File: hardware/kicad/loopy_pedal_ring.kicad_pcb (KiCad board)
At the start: 2 copper layers, 68 x 68 mm, 25 parts, among them J1 Conn_01x08

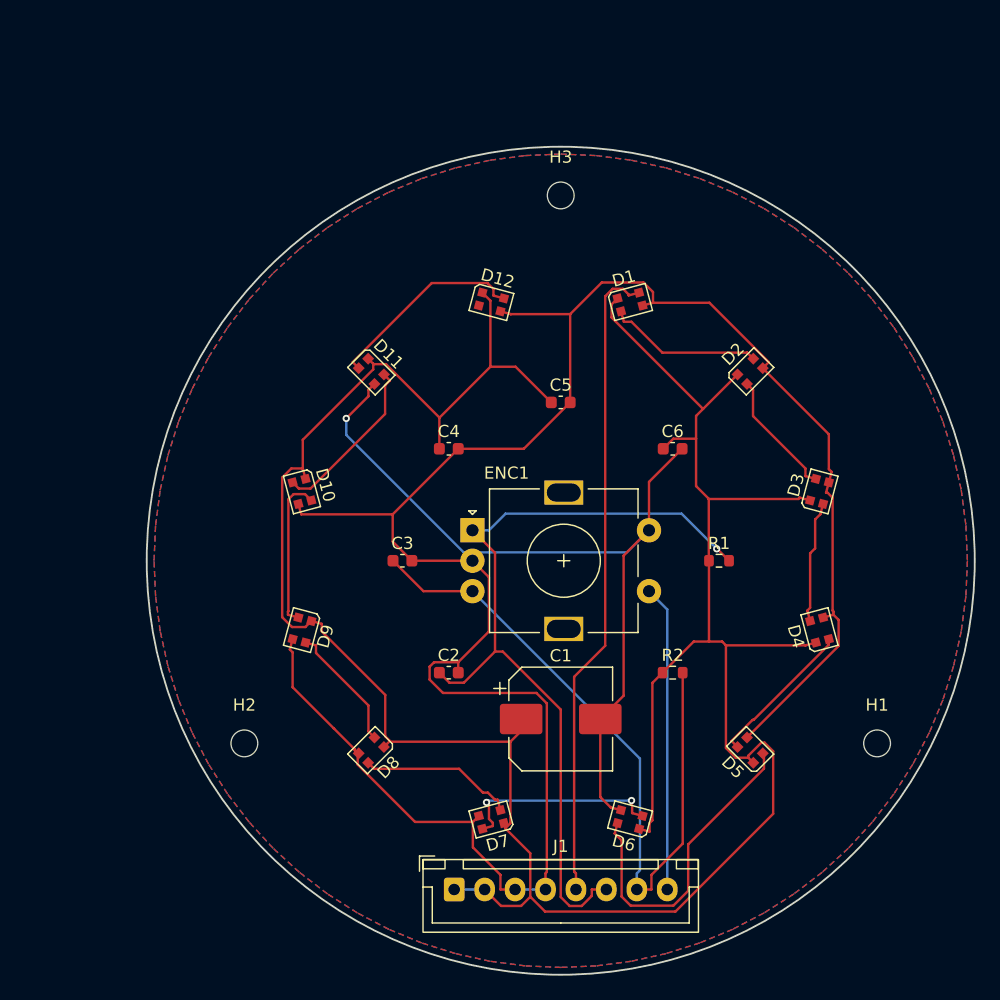
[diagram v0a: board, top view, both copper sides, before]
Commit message: feat(hardware): THT Loopy pedal main + ring boards, fab-ready
Through-hole MIDI looper foot-pedal: two KiCad 10 boards generated from
SKiDL + a scripted place/route pipeline, ready for JLCPCB bare-board fab.

Main board (94x96mm):
- Arduino Pro Micro (ATmega32U4) native USB-MIDI, buffered DIN MIDI OUT
  (74AHCT125), opto-isolated DIN MIDI IN (H11L1)
- 9V centre-negative barrel -> reverse-protection Schottky + TVS -> buck
  (+5V_LED for the LED ring); Pro Micro powered via RAW (onboard reg -> VCC)
- 10 footswitch headers, faceplate RESET (J20) + 6-pin ICSP (J21) recovery
- Fully silk-labelled (functions + component values), 4x M3 GND-bonded holes

Ring board (60mm round):
- Hosts an off-the-shelf 16-LED WS2812 NeoPixel module + EC11 encoder,
  8-pin link to the main board; 4-pad module mount (DIN/+5V/GND + DOUT post)

Both boards DRC-clean; gerbers + BOM/CPL in fab/. Vendored footprints and
3D models in loopy.pretty/. Plan-of-record in loopy_pedal_pcb_tht_plan.md.
Firmware skeleton (USB-MIDI + Serial1 DIN + footswitch debounce) in firmware/.
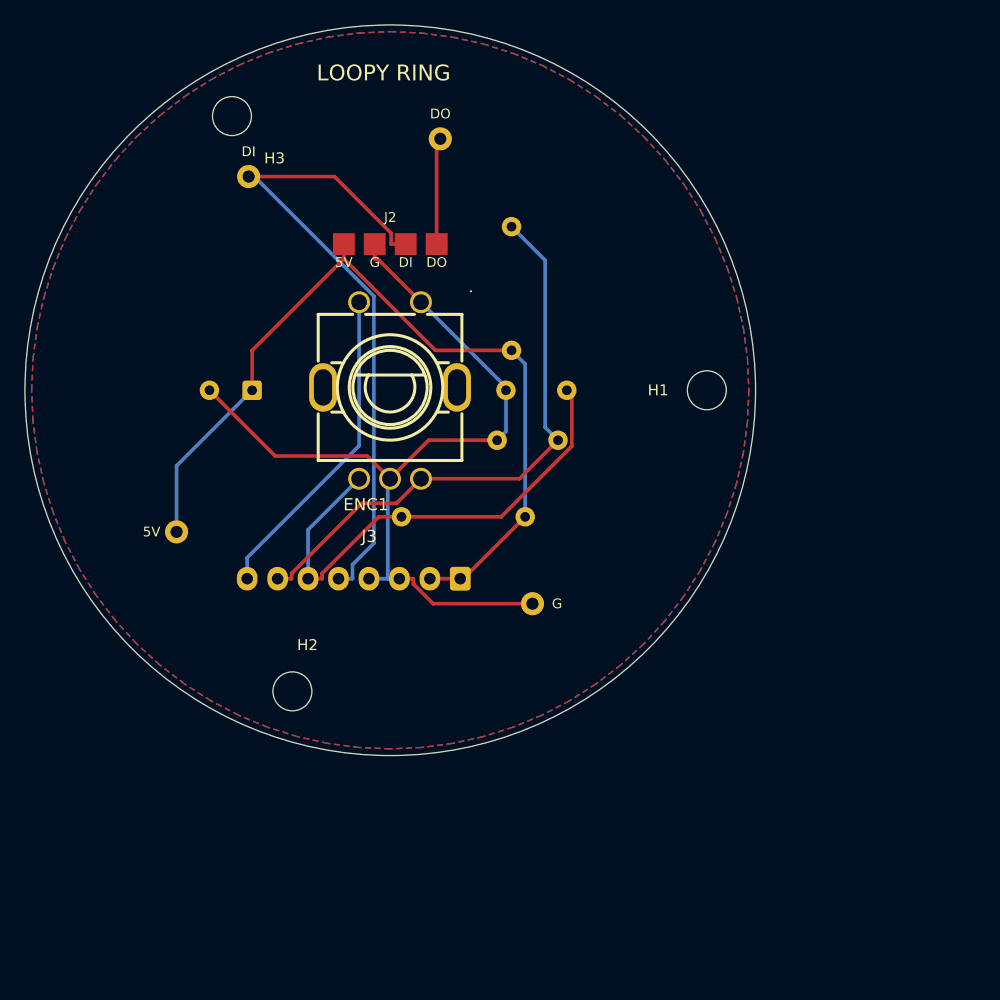
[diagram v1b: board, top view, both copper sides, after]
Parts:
- removed C4, C5, C6: 100nF, C_0603_1608Metric
- removed D1, D10, D11, D12, D2, D3, D4, D5, D6, D7, D8, D9: WS2812B, LED_WS2812B-2020_PLCC4_2.0x2.0mm
- added J2: NEOPIXEL, WirePads_1x04, F.Cu at (36.0, 24.0)
- added J3: RINGPINS, ModuleMountPads_4, F.Cu at (36.0, 36.0)
- added RING1: NeoPixel16, NeoPixel_Ring16, F.Cu at (36.0, 36.0)
- C1: value 1000uF -> 470uF; footprint CP_Elec_8x10 -> CP_Radial_D8.0mm_P3.50mm; moved to B.Cu
- C2, C3: footprint C_0603_1608Metric -> C_Disc_D5.0mm_W2.5mm_P5.00mm; moved to B.Cu
- ENC1: footprint RotaryEncoder_Alps_EC11E-Switch_Vertical_H20mm -> RotaryEncoder_EC11
- H1, H2, H3: value MountingHole_2.2mm_M2 -> MountingHole_3.2mm_M3; footprint MountingHole_2.2mm_M2 -> MountingHole_3.2mm_M3
- J1: moved to B.Cu
- R1, R2: footprint R_0603_1608Metric -> R_Axial_DIN0207_L6.3mm_D2.5mm_P10.16mm_Horizontal; moved to B.Cu
- moved C1 37.0 mm to (24.7, 36.0), turned to 180 degrees
- moved H1 32.2 mm to (62.0, 36.0)
- moved R2 29.6 mm to (46.0, 32.7), turned to 90 degrees
- moved H3 27.8 mm to (23.0, 13.5)
- moved J1 25.5 mm to (41.8, 51.5), turned to 180 degrees
- moved C2 25.1 mm to (50.5, 36.0), turned to 180 degrees
- moved R1 16.3 mm to (47.1, 46.4), turned to 180 degrees
- moved C3 16.2 mm to (49.8, 40.1), turned to 180 degrees
- moved ENC1 13.3 mm to (36.0, 36.0)
- moved H2 5.82 mm to (28.0, 60.7)
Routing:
- net GND: track 252.7 -> 71.8 mm, vias 1 -> 0
- net +5V_LED: track 223.1 -> 70.3 mm
- net ENC_A: track 67.6 -> 41.1 mm, vias 1 -> 0
- net RING_D5: track 26.5 -> 0.00 mm
- net RING_D6: track 17.0 -> 0.00 mm, vias 2 -> 0
- net RING_D11: track 16.6 -> 0.00 mm
- net RING_D10: track 14.0 -> 0.00 mm
- net RING_D1: track 12.8 -> 0.00 mm
- net RING_D7: track 12.8 -> 0.00 mm
- net RING_D9: track 12.7 -> 0.00 mm
- net RING_D4: track 12.4 -> 0.00 mm
- net ENC_B: track 57.9 -> 47.1 mm
- net RING_D2: track 10.4 -> 0.00 mm
- net RING_D8: track 10.4 -> 0.00 mm
- net RING_D3: track 10.1 -> 0.00 mm
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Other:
- board size 68 x 68 mm -> 60 x 60 mm
- board text added: "LOOPY RING"

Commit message: feat(hardware): main-board respin — on-board buck, floorplan, wide rails + ground planes
Reworked the loopy_pedal main board:
- MP1584 buck mounts flat on its own footprint (loopy:BuckModule_MP1584 + STEP),
  no longer a 1x4 header; fixed the SW_TRACK4<->R7/R8 short by relocating the
  A3-sense divider; added local decoupling C11/C16 for U1/U2.
- Floorplan: power grouped in the bottom band, MIDI on the right, Pro Micro on
  the left (USB accessible); force-directed placement + Freerouting.
- Power nets 0.8mm / +5V 0.5mm net classes, dual F.Cu+B.Cu ground planes.
- Ring board: component values onto the silkscreen.
DRC: main + ring both 0 violations, 0 unconnected.
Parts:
- ENC1: value RotaryEncoder_Switch -> EC11
- J1: value Conn_01x08 -> JST-XH 8P
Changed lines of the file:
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@@
 			)
 		)
-		(property "Value" "RotaryEncoder_Switch"
-			(at 0 11.25 0)
-			(layer "F.Fab")
-			(effects
-				(font
-					(size 1 1)
+		(property "Value" "EC11"
+			(at -11.9825 -5.0175 0)
+			(layer "F.SilkS")
+			(effects
+				(font
+					(size 0.8 0.8)
 					(thickness 0.15)
 				)
@@
 		(property "Value" "NEOPIXEL"
 			(at 0 2.6 0)
-			(layer "F.Fab")
-			(hide yes)
+			(layer "F.SilkS")
 			(effects
 				(font
@@
 		)
 		(property "Value" "RINGPINS"
-			(at 0 15 0)
-			(layer "F.Fab")
-			(hide yes)
-			(effects
-				(font
-					(size 1 1)
+			(at 12 -5 0)
+			(layer "F.SilkS")
+			(effects
+				(font
+					(size 0.8 0.8)
 					(thickness 0.15)
 				)
@@
 		(property "Value" "NeoPixel16"
 			(at 0 25 0)
-			(layer "F.Fab")
-			(hide yes)
+			(layer "F.SilkS")
 			(effects
 				(font
@@
 		)
 		(property "Value" "100nF"
-			(at 2.5 -2.5 0)
-			(layer "B.Fab")
-			(effects
-				(font
-					(size 1 1)
+			(at 0 6 0)
+			(layer "B.SilkS")
+			(effects
+				(font
+					(size 0.8 0.8)
 					(thickness 0.15)
 				)
@@
 		)
 		(property "Value" "10k"
-			(at 5.08 -2.37 0)
-			(layer "B.Fab")
-			(effects
-				(font
-					(size 1 1)
+			(at -5.92 4.3923 0)
+			(layer "B.SilkS")
+			(effects
+				(font
+					(size 0.8 0.8)
 					(thickness 0.15)
 				)
@@
 			)
 		)
-		(property "Value" "Conn_01x08"
+		(property "Value" "JST-XH 8P"
 			(at 8.75 -4.6 0)
-			(layer "B.Fab")
+			(layer "B.SilkS")
 			(effects
 				(font
@@
 		(property "Value" "10k"
 			(at 5.08 -2.37 90)
-			(layer "B.Fab")
+			(layer "B.SilkS")
 			(effects
 				(font
@@
 		(property "Value" "100nF"
 			(at 2.5 -2.5 0)
-			(layer "B.Fab")
+			(layer "B.SilkS")
 			(effects
 				(font
@@
 		(property "Value" "470uF"
 			(at 1.75 -5.25 0)
-			(layer "B.Fab")
-			(effects
-				(font
+			(layer "B.SilkS")
+			(effects
+				(font
